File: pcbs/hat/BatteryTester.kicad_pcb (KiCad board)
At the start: 2 copper layers, 153 parts, among them J1 Screw_Terminal_01x02, J2 XT60, J3 XT60, J4 XT60, J5 XT60, J6 XT60, J7 XT60, J8 XT60, J9 XT60, Q1 Q_NMOS_DGS, Q10 Q_NMOS_DGS, Q11 Q_NMOS_DGS, Q12 Q_NMOS_DGS, Q13 Q_NMOS_DGS, Q14 Q_NMOS_DGS, Q15 Q_NMOS_DGS, Q16 Q_NMOS_DGS, Q2 Q_NMOS_DGS, Q3 Q_NMOS_DGS, Q4 Q_NMOS_DGS, Q5 Q_NMOS_DGS, Q6 Q_NMOS_DGS, Q7 Q_NMOS_DGS, Q8 Q_NMOS_DGS, Q9 Q_NMOS_DGS, U1 INA181A3IDBVR, U10 TP5000_Breakout_Akaddy, U11 INA181A3IDBVR, U12 TP5000_Breakout_Akaddy, U13 INA181A3IDBVR, U14 TP5000_Breakout_Akaddy, U15 INA181A3IDBVR, U16 TP5000_Breakout_Akaddy, U17 NUCLEO-F401RE, U18 ADS7828, U19 ADS7828, U2 TP5000_Breakout_Akaddy, U20 ADS7828, U21 ???, U3 INA181A3IDBVR, U4 TP5000_Breakout_Akaddy, U5 INA181A3IDBVR, U6 TP5000_Breakout_Akaddy, U7 INA181A3IDBVR, U8 TP5000_Breakout_Akaddy, U9 INA181A3IDBVR

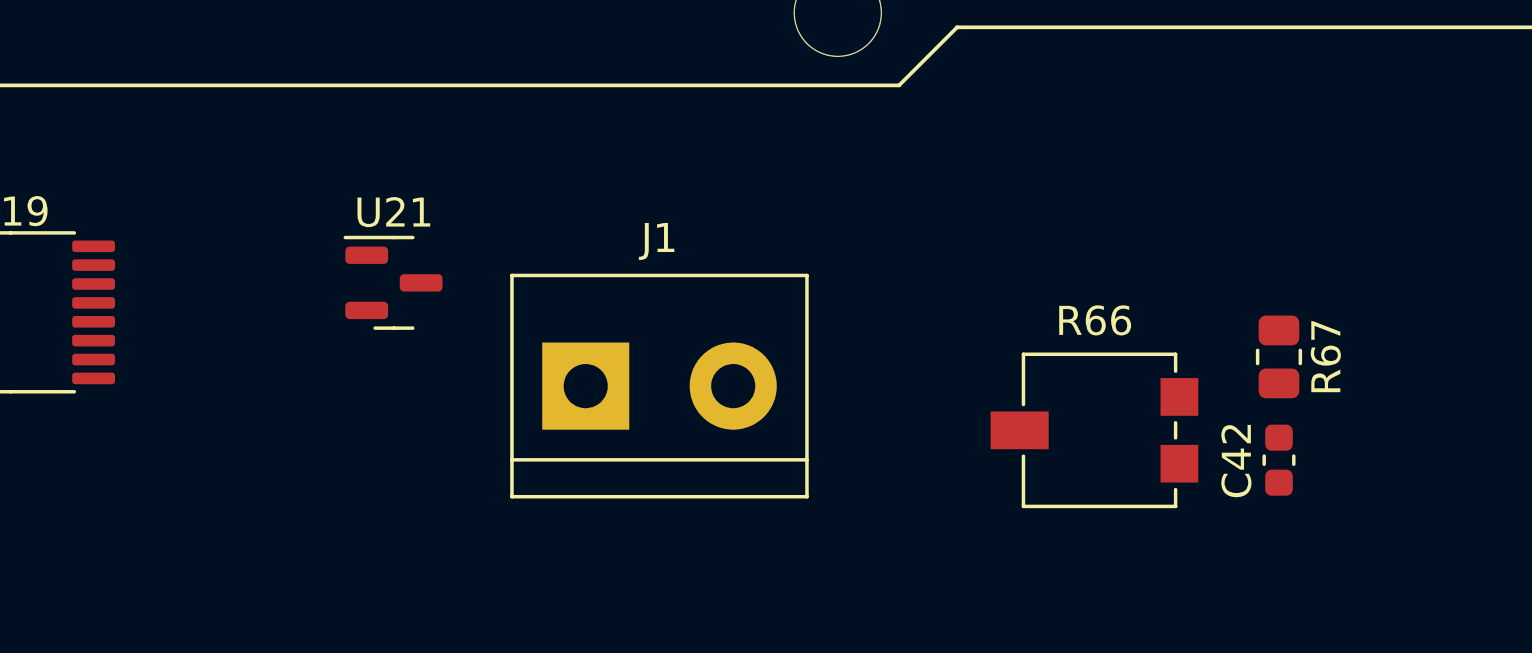
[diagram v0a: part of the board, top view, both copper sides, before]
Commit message: add vref for adc's
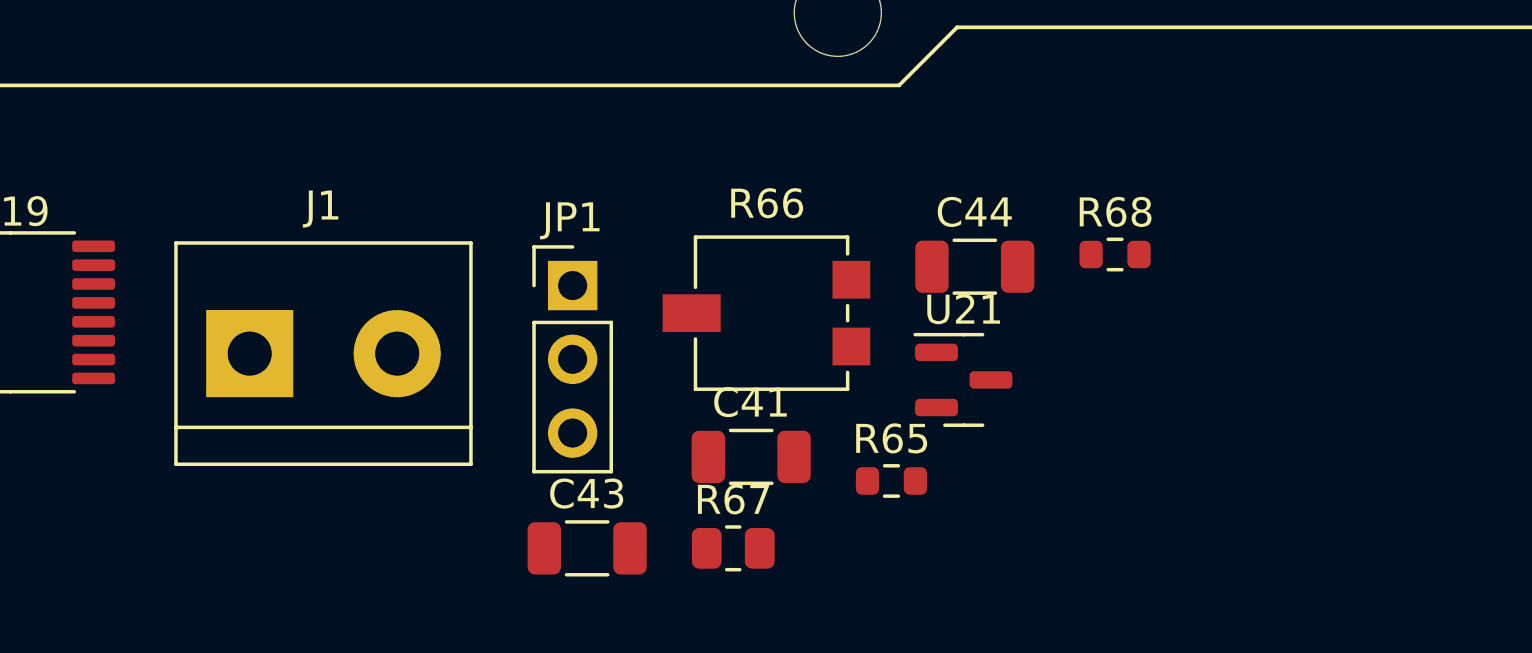
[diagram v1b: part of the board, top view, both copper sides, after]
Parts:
- removed C42: 1u, Capacitor_SMD:C_0603_1608Metric
- added C41: 22u, Capacitor_SMD:C_1206_3216Metric, F.Cu at (62.1, 115.2)
- added C43: 22u, Capacitor_SMD:C_1206_3216Metric, F.Cu at (56.4, 118.4)
- added C44: 22u, Capacitor_SMD:C_1206_3216Metric, F.Cu at (69.8, 108.7)
- added JP1: Jumper, Connector_PinHeader_2.54mm:PinHeader_1x03_P2.54mm_Vertical, F.Cu at (55.9, 109.3)
- added R65: 27, Resistor_SMD:R_0603_1608Metric, F.Cu at (66.9, 116.0)
- added R68: 27, Resistor_SMD:R_0603_1608Metric, F.Cu at (74.6, 108.2)
- U21: value ??? -> LM3480-IM3-5.0
- moved R67 19.9 mm to (61.5, 118.4), turned to 0 degrees
- moved U21 19.9 mm to (69.4, 112.6)
- moved R66 12.0 mm to (62.8, 110.3)
- moved J1 11.6 mm to (44.8, 111.7)
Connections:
- U18 pad 10: +5VA -> /Converters/ADC_Ref
- U19 pad 10: +5VA -> /Converters/ADC_Ref
- U20 pad 10: +5VA -> /Converters/ADC_Ref

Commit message: cleanup
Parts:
- moved U17 4.32 mm to (53.3, 57.9)
- moved C33 3.56 mm to (176.2, 76.6)
- moved C39 3.56 mm to (140.8, 99.3)
- moved Q1 3.56 mm to (191.5, 102.0)
- moved R31 3.56 mm to (256.1, 69.6)
- moved C14 3.56 mm to (140.8, 28.0)
- moved C29 3.56 mm to (263.0, 28.0)
- moved C19 3.56 mm to (263.0, 63.6)
- moved C24 3.56 mm to (140.8, 63.6)
- moved C8 3.56 mm to (176.2, 40.9)
- moved Q12 3.56 mm to (269.4, 20.6)
- moved Q3 3.56 mm to (191.5, 30.6)
- moved Q8 3.56 mm to (269.4, 56.3)
- moved R47 3.56 mm to (256.1, 33.9)
- moved C3 3.56 mm to (176.2, 112.2)
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
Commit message: few little change
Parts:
- removed C13, C18, C23, C28, C3, C33, C38, C8: 220u, Capacitor_THT:CP_Radial_D6.3mm_P2.50mm
- removed C41, C43: 22u, Capacitor_SMD:C_1206_3216Metric
- removed JP1: Jumper, Connector_PinHeader_2.54mm:PinHeader_1x03_P2.54mm_Vertical
- removed R59, R63: 680, Resistor_SMD:R_0603_1608Metric
- removed R60, R62, R64: 10k, Resistor_SMD:R_0603_1608Metric
- removed R61: 3k3, Resistor_SMD:R_0603_1608Metric
- removed R65, R68: 27, Resistor_SMD:R_0603_1608Metric
- removed R66: TS53YL503MR10, Potentiometer_SMD:Potentiometer_Vishay_TS53YL_Vertical
- removed R67: 25k, Resistor_SMD:R_0805_2012Metric
- added C45: 47u, Capacitor_SMD:C_1206_3216Metric, F.Cu at (60.4, 115.4)
- added C46: 22u, Capacitor_SMD:C_1206_3216Metric, F.Cu at (60.4, 112.1)
- added C47: 22u, Capacitor_SMD:C_1206_3216Metric, F.Cu at (60.4, 108.7)
- added U22: LM3480-IM3-5.0, Package_TO_SOT_SMD:SOT-23, F.Cu at (65.7, 112.6)
- C1, C11, C16, C21, C26, C31, C36, C6: value 100n -> 200n
- C14, C19, C24, C29, C34, C39, C4, C9: value 1µ -> 15u; footprint Capacitor_SMD:C_0603_1608Metric -> Capacitor_SMD:C_0805_2012Metric
- C44: value 22u -> 47u
- J2, J3, J4, J5, J6, J7, J8, J9: footprint Connector_AMASS:AMASS_XT60-M_1x02_P7.20mm_Vertical -> Connector_Phoenix_MSTB:PhoenixContact_MSTBA_2,5_2-G-5,08_1x02_P5.08mm_Horizontal
- R1, R33: value CST0612-FC-R005E (5mΩ) -> 680; footprint STS_Resistor_SMD:CST0612-FC-R002E -> Resistor_SMD:R_0603_1608Metric
- R10, R34, R42: value 1 -> 10k; footprint Resistor_THT:R_Axial_DIN0617_L17.0mm_D6.0mm_P25.40mm_Horizontal -> Resistor_SMD:R_0603_1608Metric
- R11, R39: value 680 -> 1k
- R12, R22, R36, R40, R54, R8: value 10k -> 680
- R13, R21, R45: value 3k3 -> 10k
- R16, R30, R44: value 10k -> CST0612-FC-R005E (5mΩ); footprint Resistor_SMD:R_0603_1608Metric -> STS_Resistor_SMD:CST0612-FC-R002E
- R17, R41, R49: value CST0612-FC-R005E (5mΩ) -> 10k; footprint STS_Resistor_SMD:CST0612-FC-R002E -> Resistor_SMD:R_0603_1608Metric
- R18: value 1 -> 1k; footprint Resistor_THT:R_Axial_DIN0617_L17.0mm_D6.0mm_P25.40mm_Horizontal -> Resistor_SMD:R_0603_1608Metric
- R2: value 1 -> CST0612-FC-R005E (5mΩ); footprint Resistor_THT:R_Axial_DIN0617_L17.0mm_D6.0mm_P25.40mm_Horizontal -> STS_Resistor_SMD:CST0612-FC-R002E
- R23, R51: value 680 -> CST0612-FC-R005E (5mΩ); footprint Resistor_SMD:R_0603_1608Metric -> STS_Resistor_SMD:CST0612-FC-R002E
- R25: value CST0612-FC-R005E (5mΩ) -> 1k; footprint STS_Resistor_SMD:CST0612-FC-R002E -> Resistor_SMD:R_0603_1608Metric
- R26, R50: value 1 -> 680; footprint Resistor_THT:R_Axial_DIN0617_L17.0mm_D6.0mm_P25.40mm_Horizontal -> Resistor_SMD:R_0603_1608Metric
- R27, R3, R31, R35, R55, R7: value 680 -> 10k
- R29, R5: value 3k3 -> 680
- R32, R4, R46: value 10k -> 1k
- R37: value 3k3 -> CST0612-FC-R005E (5mΩ); footprint Resistor_SMD:R_0603_1608Metric -> STS_Resistor_SMD:CST0612-FC-R002E
- R53: value 3k3 -> 1k
- R57: value CST0612-FC-R005E (5mΩ) -> 100; footprint STS_Resistor_SMD:CST0612-FC-R002E -> Resistor_SMD:R_0603_1608Metric
- R58: value 1 -> 100; footprint Resistor_THT:R_Axial_DIN0617_L17.0mm_D6.0mm_P25.40mm_Horizontal -> Resistor_SMD:R_0603_1608Metric
- U1, U11, U13, U15, U3, U5, U7, U9: value INA181A3IDBVR -> INA181A2IDBVR
- U21: value LM3480-IM3-5.0 -> AP2138N-2.5TRG1
- moved R40 146.6 mm to (260.5, 25.3)
- moved R36 140.6 mm to (249.9, 32.3)
- moved R37 140.4 mm to (241.9, 23.2)
- moved R31 130.1 mm to (126.1, 75.2)
- moved R24 128.2 mm to (236.4, 75.2)
- moved R22 125.6 mm to (249.9, 64.6)
- moved R32 119.3 mm to (122.1, 75.2)
- moved R30 119.1 mm to (131.6, 55.6)
- moved R38 115.7 mm to (236.4, 42.8)
- moved R23 110.2 mm to (241.9, 55.6)
- moved R39 102.1 mm to (232.4, 42.8)
- moved R29 98.4 mm to (139.6, 64.6)
- moved R46 78.3 mm to (177.2, 75.2)
- moved R56 78.1 mm to (118.0, 109.2)
- moved R55 71.7 mm to (134.1, 107.5)
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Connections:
- C1 pad 1: GND -> Net-(C1-Pad1)
- C1 pad 2: +5V -> GND
- C11 pad 1: GND -> Net-(C11-Pad1)
- C11 pad 2: +5V -> GND
- C12 pad 1: Net-(C12-Pad1) -> GND
- C12 pad 2: GND -> +5V
- C16 pad 1: GND -> Net-(C16-Pad1)
- C16 pad 2: +5V -> GND
- C17 pad 1: Net-(C17-Pad1) -> GND
- C17 pad 2: GND -> +5V
- C2 pad 1: Net-(C2-Pad1) -> GND
- C2 pad 2: GND -> +5V
- C21 pad 1: GND -> Net-(C21-Pad1)
- C21 pad 2: +5V -> GND
- C22 pad 1: Net-(C22-Pad1) -> GND
- C22 pad 2: GND -> +5V
- C26 pad 1: GND -> Net-(C26-Pad1)
- C26 pad 2: +5V -> GND
- C27 pad 1: Net-(C27-Pad1) -> GND
- C27 pad 2: GND -> +5V
- C31 pad 1: GND -> Net-(C31-Pad1)
- C31 pad 2: +5V -> GND
- C32 pad 1: Net-(C32-Pad1) -> GND
- C32 pad 2: GND -> +5V
- C36 pad 1: GND -> Net-(C36-Pad1)
- C36 pad 2: +5V -> GND
- C37 pad 1: Net-(C37-Pad1) -> GND
- C37 pad 2: GND -> +5V
- C44 pad 2: +5VA -> Net-(C44-Pad2)
- C6 pad 1: GND -> Net-(C6-Pad1)
- C6 pad 2: +5V -> GND
- C7 pad 1: Net-(C7-Pad1) -> GND
- C7 pad 2: GND -> +5V
- Q1 pad 1: Net-(C3-Pad1) -> /SENSOR_10
- Q1 pad 2: Net-(C2-Pad1) -> Net-(C1-Pad1)
- Q11 pad 1: Net-(C28-Pad1) -> /SENSOR_80
- Q11 pad 2: Net-(C27-Pad1) -> Net-(C26-Pad1)
- Q13 pad 1: Net-(C33-Pad1) -> /SENSOR_70
- Q13 pad 2: Net-(C32-Pad1) -> Net-(C31-Pad1)
- Q15 pad 1: Net-(C38-Pad1) -> /SENSOR_60
- Q15 pad 2: Net-(C37-Pad1) -> Net-(C36-Pad1)
- Q3 pad 1: Net-(C8-Pad1) -> /SENSOR_20
- Q3 pad 2: Net-(C7-Pad1) -> Net-(C6-Pad1)
- Q5 pad 1: Net-(C13-Pad1) -> /SENSOR_30
- Q5 pad 2: Net-(C12-Pad1) -> Net-(C11-Pad1)
- Q7 pad 1: Net-(C18-Pad1) -> /SENSOR_40
- Q7 pad 2: Net-(C17-Pad1) -> Net-(C16-Pad1)
- Q9 pad 1: Net-(C23-Pad1) -> /SENSOR_50
- Q9 pad 2: Net-(C22-Pad1) -> Net-(C21-Pad1)
- R1 pad 1: /test-battery-1/GNDBAT -> /SIGNAL_11
- R1 pad 2: Net-(R1-Pad2) -> Net-(C1-Pad1)
- R10 pad 1: Net-(C8-Pad1) -> Net-(C6-Pad1)
- R10 pad 2: /SENSOR_20 -> GND
- R11 pad 1: /SIGNAL_21 -> Net-(R11-Pad1)
- R11 pad 2: Net-(C7-Pad1) -> /SENSOR_21
- R12 pad 1: Net-(C7-Pad1) -> /SIGNAL_20
- R12 pad 2: GND -> Net-(Q4-Pad2)
- R13 pad 1: Net-(R13-Pad1) -> /SENSOR_22
- R13 pad 2: /SENSOR_21 -> GND
- R14 pad 1: /SENSOR_22 -> Net-(Q4-Pad2)
- R15 pad 1: /SIGNAL_20 -> /SIGNAL_31
- R15 pad 2: Net-(Q4-Pad2) -> Net-(C11-Pad1)
- R16 pad 1: Net-(Q4-Pad2) -> /test-battery-3/GNDBAT
- R16 pad 2: GND -> Net-(R16-Pad2)
- R17 pad 1: /test-battery-3/GNDBAT -> Net-(C11-Pad1)
- R17 pad 2: Net-(R17-Pad2) -> GND
- R18 pad 1: Net-(C13-Pad1) -> Net-(R18-Pad1)
- R18 pad 2: /SENSOR_30 -> /SENSOR_31
- R19 pad 1: /SIGNAL_31 -> /SIGNAL_30
- R19 pad 2: Net-(C12-Pad1) -> Net-(Q6-Pad2)
- R2 pad 1: Net-(C3-Pad1) -> /test-battery-1/GNDBAT
- R2 pad 2: /SENSOR_10 -> Net-(R2-Pad2)
- R20 pad 1: Net-(C12-Pad1) -> /SENSOR_32
- R21 pad 1: Net-(R21-Pad1) -> Net-(Q6-Pad2)
- R21 pad 2: /SENSOR_31 -> GND
- R22 pad 1: /SENSOR_32 -> /SIGNAL_41
- R22 pad 2: GND -> Net-(C16-Pad1)
- R23 pad 1: /SIGNAL_30 -> /test-battery-4/GNDBAT
- R23 pad 2: Net-(Q6-Pad2) -> Net-(R23-Pad2)
- R24 pad 1: Net-(Q6-Pad2) -> Net-(C16-Pad1)
- R25 pad 1: /test-battery-4/GNDBAT -> Net-(R25-Pad1)
- R25 pad 2: Net-(R25-Pad2) -> /SENSOR_41
- R26 pad 1: Net-(C18-Pad1) -> /SIGNAL_40
- R26 pad 2: /SENSOR_40 -> Net-(Q8-Pad2)
- R27 pad 1: /SIGNAL_41 -> /SENSOR_42
- R27 pad 2: Net-(C17-Pad1) -> GND
- R28 pad 1: Net-(C17-Pad1) -> Net-(Q8-Pad2)
- R29 pad 1: Net-(R29-Pad1) -> /SIGNAL_51
- R29 pad 2: /SENSOR_41 -> Net-(C21-Pad1)
- R3 pad 1: /SIGNAL_11 -> Net-(C1-Pad1)
- R3 pad 2: Net-(C2-Pad1) -> GND
- R30 pad 1: /SENSOR_42 -> /test-battery-5/GNDBAT
- R30 pad 2: GND -> Net-(R30-Pad2)
- R31 pad 1: /SIGNAL_40 -> Net-(C21-Pad1)
- R31 pad 2: Net-(Q8-Pad2) -> GND
- R32 pad 1: Net-(Q8-Pad2) -> Net-(R32-Pad1)
- R32 pad 2: GND -> /SENSOR_51
- R33 pad 1: /test-battery-5/GNDBAT -> /SIGNAL_50
- R33 pad 2: Net-(R33-Pad2) -> Net-(Q10-Pad2)
- R34 pad 1: Net-(C23-Pad1) -> /SENSOR_52
- R34 pad 2: /SENSOR_50 -> GND
- R35 pad 1: /SIGNAL_51 -> Net-(Q10-Pad2)
- R35 pad 2: Net-(C22-Pad1) -> GND
- R36 pad 1: Net-(C22-Pad1) -> /SIGNAL_81
- R36 pad 2: GND -> Net-(C26-Pad1)
- R37 pad 1: Net-(R37-Pad1) -> /test-battery-8/GNDBAT
- R37 pad 2: /SENSOR_51 -> Net-(R37-Pad2)
- R38 pad 1: /SENSOR_52 -> Net-(C26-Pad1)
- R39 pad 1: /SIGNAL_50 -> Net-(R39-Pad1)
- R39 pad 2: Net-(Q10-Pad2) -> /SENSOR_81
- R4 pad 1: Net-(C2-Pad1) -> Net-(R4-Pad1)
- R4 pad 2: GND -> /SENSOR_11
- R40 pad 1: Net-(Q10-Pad2) -> /SIGNAL_80
- R40 pad 2: GND -> Net-(Q12-Pad2)
- R41 pad 1: /test-battery-8/GNDBAT -> /SENSOR_82
- R41 pad 2: Net-(R41-Pad2) -> GND
- R42 pad 1: Net-(C28-Pad1) -> Net-(Q12-Pad2)
- R42 pad 2: /SENSOR_80 -> GND
- R43 pad 1: /SIGNAL_81 -> /SIGNAL_71
- R43 pad 2: Net-(C27-Pad1) -> Net-(C31-Pad1)
- R44 pad 1: Net-(C27-Pad1) -> /test-battery-7/GNDBAT
- R44 pad 2: GND -> Net-(R44-Pad2)
- R45 pad 1: Net-(R45-Pad1) -> Net-(C31-Pad1)
- R45 pad 2: /SENSOR_81 -> GND
- R46 pad 1: /SENSOR_82 -> Net-(R46-Pad1)
- R46 pad 2: GND -> /SENSOR_71
- R47 pad 1: /SIGNAL_80 -> /SIGNAL_70
- R47 pad 2: Net-(Q12-Pad2) -> Net-(Q14-Pad2)
- R48 pad 1: Net-(Q12-Pad2) -> /SENSOR_72
- R49 pad 1: /test-battery-7/GNDBAT -> Net-(Q14-Pad2)
- R49 pad 2: Net-(R49-Pad2) -> GND
- R5 pad 1: Net-(R5-Pad1) -> /SIGNAL_10
- R5 pad 2: /SENSOR_11 -> Net-(Q2-Pad2)
- R50 pad 1: Net-(C33-Pad1) -> /SIGNAL_61
- R50 pad 2: /SENSOR_70 -> Net-(C36-Pad1)
- R51 pad 1: /SIGNAL_71 -> /test-battery-6/GNDBAT
- R51 pad 2: Net-(C32-Pad1) -> Net-(R51-Pad2)
- R52 pad 1: Net-(C32-Pad1) -> Net-(C36-Pad1)
- R53 pad 2: /SENSOR_71 -> /SENSOR_61
- R54 pad 1: /SENSOR_72 -> /SIGNAL_60
- R54 pad 2: GND -> Net-(Q16-Pad2)
- R55 pad 1: /SIGNAL_70 -> /SENSOR_62
- R55 pad 2: Net-(Q14-Pad2) -> GND
- R56 pad 1: Net-(Q14-Pad2) -> Net-(Q16-Pad2)
- R57 pad 1: /test-battery-6/GNDBAT -> +5V
- R57 pad 2: Net-(R57-Pad2) -> Net-(C44-Pad2)
- R58 pad 1: Net-(C38-Pad1) -> VCC
- R58 pad 2: /SENSOR_60 -> Net-(C45-Pad2)
- R7 pad 1: /SIGNAL_10 -> Net-(Q2-Pad2)
- R7 pad 2: Net-(Q2-Pad2) -> GND
- R8 pad 1: Net-(Q2-Pad2) -> /SIGNAL_21
- R8 pad 2: GND -> Net-(C6-Pad1)
- U1 pad 1: Net-(R5-Pad1) -> Net-(R4-Pad1)
- U1 pad 3: Net-(R1-Pad2) -> Net-(R2-Pad2)
- U1 pad 4: Net-(R1-Pad3) -> Net-(R2-Pad3)
- U11 pad 1: Net-(R45-Pad1) -> Net-(R39-Pad1)
- U11 pad 3: Net-(R41-Pad2) -> Net-(R37-Pad2)
- U11 pad 4: Net-(R41-Pad3) -> Net-(R37-Pad3)
- U13 pad 1: Net-(R53-Pad1) -> Net-(R46-Pad1)
- U13 pad 3: Net-(R49-Pad2) -> Net-(R44-Pad2)
- U13 pad 4: Net-(R49-Pad3) -> Net-(R44-Pad3)
- U15 pad 1: Net-(R61-Pad1) -> Net-(R53-Pad1)
- U15 pad 3: Net-(R57-Pad2) -> Net-(R51-Pad2)
- U15 pad 4: Net-(R57-Pad3) -> Net-(R51-Pad3)
- U21 pad 1: Net-(C41-Pad2) -> Net-(C44-Pad2)
- U21 pad 2: +5VA -> Vref_I_SENS
- U3 pad 1: Net-(R13-Pad1) -> Net-(R11-Pad1)
- U5 pad 1: Net-(R21-Pad1) -> Net-(R18-Pad1)
- U5 pad 3: Net-(R17-Pad2) -> Net-(R16-Pad2)
- U5 pad 4: Net-(R17-Pad3) -> Net-(R16-Pad3)
- U7 pad 1: Net-(R29-Pad1) -> Net-(R25-Pad1)
- U7 pad 3: Net-(R25-Pad2) -> Net-(R23-Pad2)
- U7 pad 4: Net-(R25-Pad3) -> Net-(R23-Pad3)
- U9 pad 1: Net-(R37-Pad1) -> Net-(R32-Pad1)
- U9 pad 3: Net-(R33-Pad2) -> Net-(R30-Pad2)
- U9 pad 4: Net-(R33-Pad3) -> Net-(R30-Pad3)

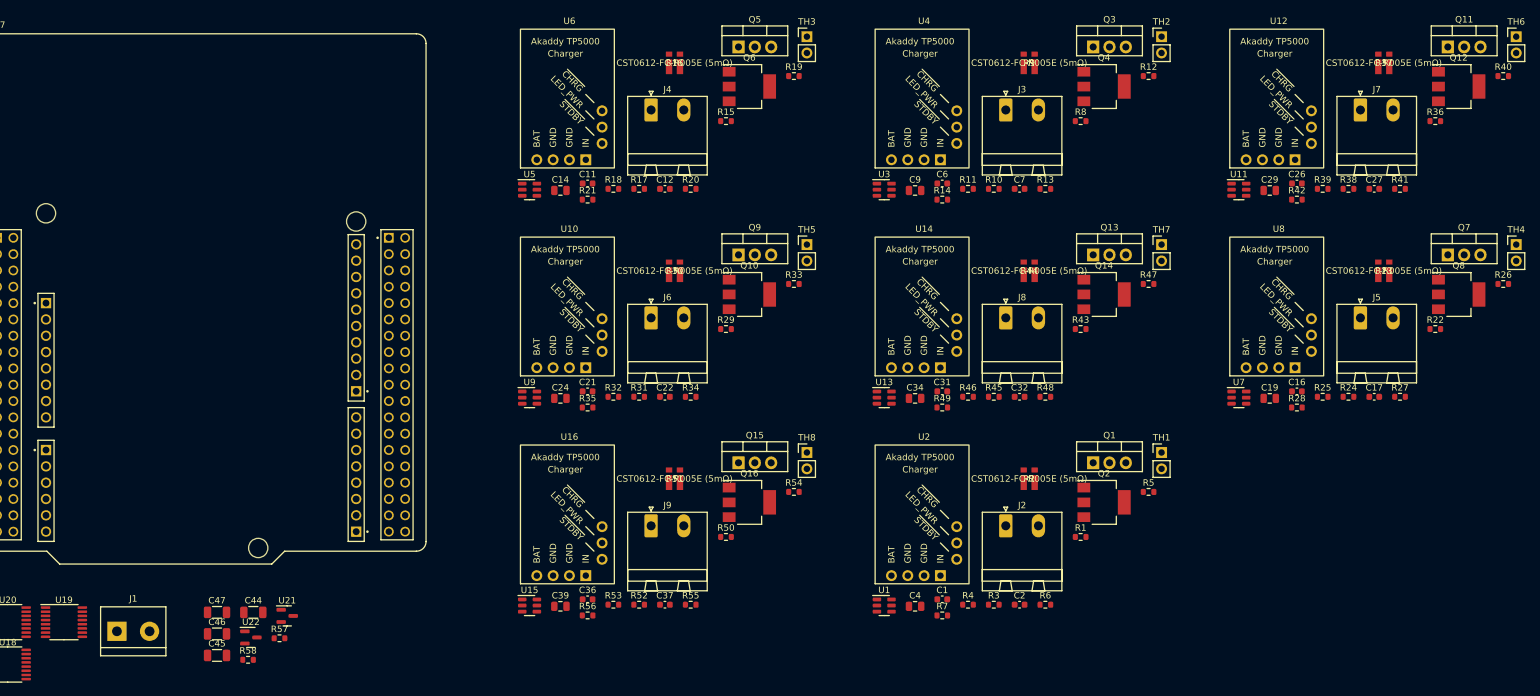
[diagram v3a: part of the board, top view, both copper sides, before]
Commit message: add memory + check footprints
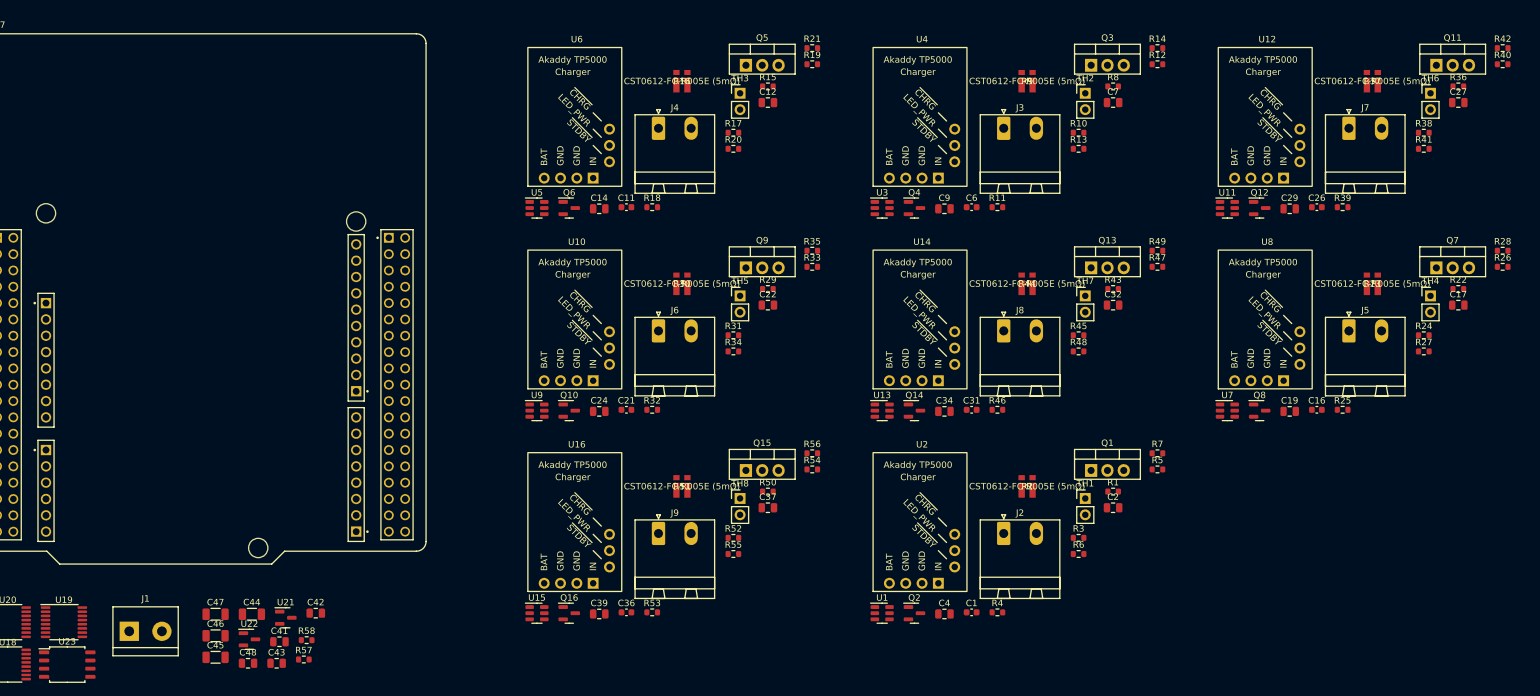
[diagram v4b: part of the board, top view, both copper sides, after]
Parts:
- added C41: 100n, Capacitor_SMD:C_0805_2012Metric, F.Cu at (70.1, 113.3)
- added C42: 100n, Capacitor_SMD:C_0805_2012Metric, F.Cu at (75.8, 108.8)
- added C43: 100n, Capacitor_SMD:C_0805_2012Metric, F.Cu at (69.7, 116.6)
- added C48: 100n, Capacitor_SMD:C_0805_2012Metric, F.Cu at (65.2, 116.6)
- added U23: SST25VF016B, Package_SO:SOIC-8_5.275x5.275mm_P1.27mm, F.Cu at (37.1, 116.8)
- C12, C17, C2, C22, C27, C32, C37, C7: footprint Capacitor_SMD:C_0603_1608Metric -> Capacitor_SMD:C_0805_2012Metric
- Q1, Q11, Q13, Q15, Q3, Q5, Q7, Q9: value Q_NMOS_DGS -> DMT6009LCT
- Q10, Q12, Q14, Q16, Q2, Q4, Q6, Q8: value Q_NMOS_DGS -> AO3414; footprint Package_TO_SOT_SMD:SOT-223 -> Package_TO_SOT_SMD:SOT-23
- moved R56 43.1 mm to (153.0, 84.0)
- moved R35 42.6 mm to (153.0, 52.4)
- moved R21 42.2 mm to (153.0, 20.9)
- moved R7 41.9 mm to (206.7, 84.0)
- moved R49 41.4 mm to (206.7, 52.4)
- moved R14 40.9 mm to (206.7, 20.9)
- moved R28 40.2 mm to (260.4, 52.4)
- moved R42 39.8 mm to (260.4, 20.9)
- moved Q12 36.3 mm to (222.6, 45.8)
- moved Q8 35.9 mm to (222.6, 77.3)
- moved Q4 35.0 mm to (168.9, 45.8)
- moved Q14 34.6 mm to (168.9, 77.3)
- moved Q2 34.2 mm to (168.9, 108.8)
- moved Q6 33.8 mm to (115.2, 45.8)
- moved Q10 33.3 mm to (115.2, 77.3)
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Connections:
- net /Board/SCL renamed /Board/ADC_SCL
- net /Board/SDA renamed /Board/ADC_SDA
- Q1 pad 1: /SENSOR_10 -> Net-(C1-Pad1)
- Q1 pad 2: Net-(C1-Pad1) -> /SENSOR_10
- Q11 pad 1: /SENSOR_80 -> Net-(C26-Pad1)
- Q11 pad 2: Net-(C26-Pad1) -> /SENSOR_80
- Q13 pad 1: /SENSOR_70 -> Net-(C31-Pad1)
- Q13 pad 2: Net-(C31-Pad1) -> /SENSOR_70
- Q15 pad 1: /SENSOR_60 -> Net-(C36-Pad1)
- Q15 pad 2: Net-(C36-Pad1) -> /SENSOR_60
- Q3 pad 1: /SENSOR_20 -> Net-(C6-Pad1)
- Q3 pad 2: Net-(C6-Pad1) -> /SENSOR_20
- Q5 pad 1: /SENSOR_30 -> Net-(C11-Pad1)
- Q5 pad 2: Net-(C11-Pad1) -> /SENSOR_30
- Q7 pad 1: /SENSOR_40 -> Net-(C16-Pad1)
- Q7 pad 2: Net-(C16-Pad1) -> /SENSOR_40
- Q9 pad 1: /SENSOR_50 -> Net-(C21-Pad1)
- Q9 pad 2: Net-(C21-Pad1) -> /SENSOR_50
- R12 pad 2: Net-(Q4-Pad2) -> Net-(Q4-Pad1)
- R14 pad 1: Net-(Q4-Pad2) -> Net-(Q4-Pad1)
- R19 pad 2: Net-(Q6-Pad2) -> Net-(Q6-Pad1)
- R21 pad 1: Net-(Q6-Pad2) -> Net-(Q6-Pad1)
- R26 pad 2: Net-(Q8-Pad2) -> Net-(Q8-Pad1)
- R28 pad 1: Net-(Q8-Pad2) -> Net-(Q8-Pad1)
- R33 pad 2: Net-(Q10-Pad2) -> Net-(Q10-Pad1)
- R35 pad 1: Net-(Q10-Pad2) -> Net-(Q10-Pad1)
- R40 pad 2: Net-(Q12-Pad2) -> Net-(Q12-Pad1)
- R42 pad 1: Net-(Q12-Pad2) -> Net-(Q12-Pad1)
- R47 pad 2: Net-(Q14-Pad2) -> Net-(Q14-Pad1)
- R49 pad 1: Net-(Q14-Pad2) -> Net-(Q14-Pad1)
- R5 pad 2: Net-(Q2-Pad2) -> Net-(Q2-Pad1)
- R54 pad 2: Net-(Q16-Pad2) -> Net-(Q16-Pad1)
- R56 pad 1: Net-(Q16-Pad2) -> Net-(Q16-Pad1)
- R7 pad 1: Net-(Q2-Pad2) -> Net-(Q2-Pad1)
- U10 pad 2: Net-(Q10-Pad1) -> Net-(Q10-Pad2)
- U10 pad 4: Net-(Q10-Pad1) -> Net-(Q10-Pad2)
- U12 pad 2: Net-(Q12-Pad1) -> Net-(Q12-Pad2)
- U12 pad 4: Net-(Q12-Pad1) -> Net-(Q12-Pad2)
- U14 pad 2: Net-(Q14-Pad1) -> Net-(Q14-Pad2)
- U14 pad 4: Net-(Q14-Pad1) -> Net-(Q14-Pad2)
- U16 pad 2: Net-(Q16-Pad1) -> Net-(Q16-Pad2)
- U16 pad 4: Net-(Q16-Pad1) -> Net-(Q16-Pad2)
- U17 pad CN10_25: unconnected-(U17-PadCN10_25) -> /Board/MEM_SCK
- U17 pad CN7_35: unconnected-(U17-PadCN7_35) -> /Board/MEM_MISO
- U17 pad CN7_36: unconnected-(U17-PadCN7_36) -> /Board/~{MEM_CE}
- U17 pad CN7_37: unconnected-(U17-PadCN7_37) -> /Board/MEM_MOSI
- U2 pad 2: Net-(Q2-Pad1) -> Net-(Q2-Pad2)
- U2 pad 4: Net-(Q2-Pad1) -> Net-(Q2-Pad2)
- U4 pad 2: Net-(Q4-Pad1) -> Net-(Q4-Pad2)
- U4 pad 4: Net-(Q4-Pad1) -> Net-(Q4-Pad2)
- U6 pad 2: Net-(Q6-Pad1) -> Net-(Q6-Pad2)
- U6 pad 4: Net-(Q6-Pad1) -> Net-(Q6-Pad2)
- U8 pad 2: Net-(Q8-Pad1) -> Net-(Q8-Pad2)
- U8 pad 4: Net-(Q8-Pad1) -> Net-(Q8-Pad2)
